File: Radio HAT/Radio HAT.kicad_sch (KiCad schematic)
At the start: 26 parts, among them J1 Raspberry_Pi_2_3, J2 Coax SMA, J3 Barrel_Jack, J4 VCC, J5 6V, J6 GND, U1 RFM98PW, U2 AZ2185D-ADJTRG1

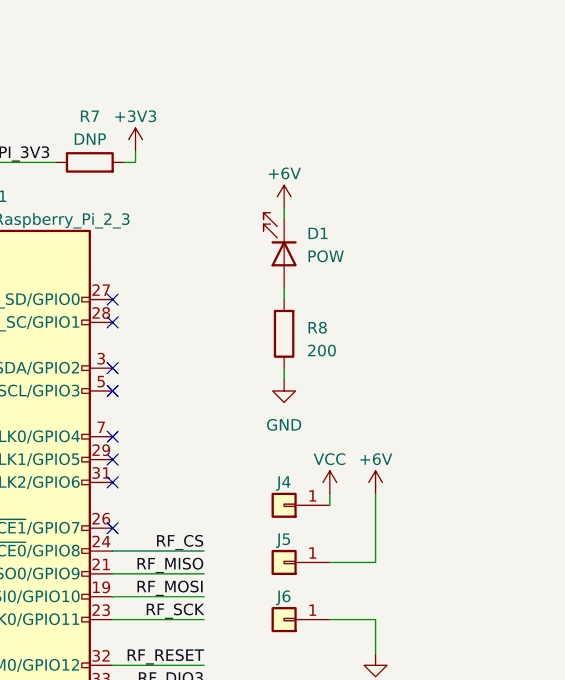
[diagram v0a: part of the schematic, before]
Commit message: Radio HAT v1.1 redesign
Changes:
- Board is back to PWR-GND-SIG-GND
- Made small electrical changes in a lot of spots with Jason
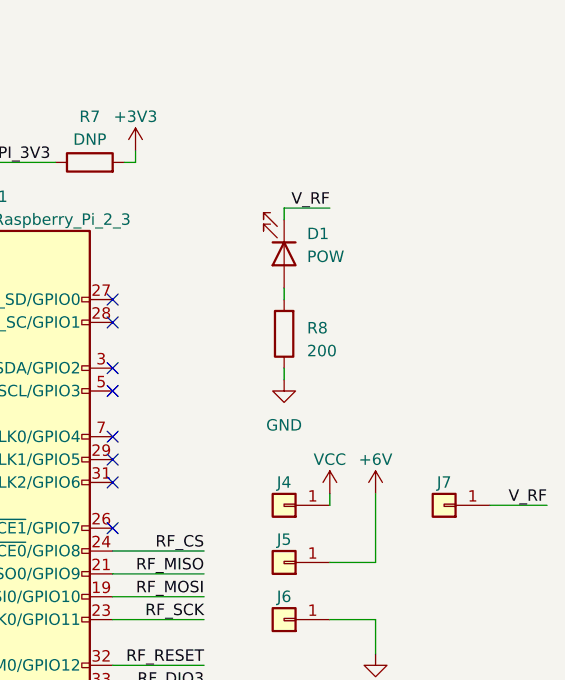
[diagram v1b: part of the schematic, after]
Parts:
- added J7: V_RF, TestPoint:TestPoint_Loop_D2.50mm_Drill1.0mm, symbol Connector_Generic:Conn_01x01
- R5: footprint Resistor_SMD:R_1206_3216Metric_Pad1.30x1.75mm_HandSolder -> Resistor_SMD:R_1210_3225Metric_Pad1.30x2.65mm_HandSolder
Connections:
- net +6V: no longer D1.1 (K)
- net V_RF: now also D1.1 (K), J7.1 (Pin_1)
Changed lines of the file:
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@@
   (title_block
     (title "Argus-1 Ground Station")
-    (date "2023-10-31")
+    (date "2023-11-10")
     (rev "v1.1")
     (company "LICENSE: CC BY 4.0")
@@
     (stroke (width 0) (type default))
   )
+  (wire (pts (xy 217.17 72.39) (xy 222.25 72.39))
+    (stroke (width 0) (type default))
+  )
   (wire (pts (xy 180.34 142.24) (xy 182.88 142.24))
     (stroke (width 0) (type default))
@@
   )
   (wire (pts (xy 147.32 100.33) (xy 157.48 100.33))
+    (stroke (width 0) (type default))
+  )
+  (wire (pts (xy 240.03 105.41) (xy 246.38 105.41))
     (stroke (width 0) (type default))
   )
@@
     (effects (font (size 1.27 1.27)) (justify left bottom))
   )
+  (label "V_RF" (at 246.38 105.41 180) (fields_autoplaced)
+    (effects (font (size 1.27 1.27)) (justify right bottom))
+  )
   (label "RF_DIO3" (at 124.46 119.38 180) (fields_autoplaced)
     (effects (font (size 1.27 1.27)) (justify right bottom))
@@
     (effects (font (size 1.27 1.27)) (justify left bottom))
   )
+  (label "V_RF" (at 222.25 72.39 180) (fields_autoplaced)
+    (effects (font (size 1.27 1.27)) (justify right bottom))
+  )
   (label "RF_DIO0" (at 73.66 129.54 0) (fields_autoplaced)
     (effects (font (size 1.27 1.27)) (justify left bottom))
@@
         (path "/e833ba5c-90ae-4111-9eec-1a872963763a"
           (reference "#PWR011") (unit 1)
+        )
+      )
+    )
+  )
+  (symbol (lib_id "Connector_Generic:Conn_01x01") (at 234.95 105.41 180) (unit 1)
+    (in_bom yes) (on_board yes) (dnp no)
+    (property "Reference" "J7" (at 234.95 102.87 0)
+      (effects (font (size 1.27 1.27)))
+    )
+    (property "Value" "V_RF" (at 234.95 102.87 0)
+      (effects (font (size 1.27 1.27)) hide)
+    )
+    (property "Footprint" "TestPoint:TestPoint_Loop_D2.50mm_Drill1.0mm" (at 234.95 105.41 0)
+      (effects (font (size 1.27 1.27)) hide)
+    )
+    (property "Datasheet" "~" (at 234.95 105.41 0)
+      (effects (font (size 1.27 1.27)) hide)
+    )
+    (pin "1")
+    (instances
+      (project "Radio HAT"
+        (path "/e833ba5c-90ae-4111-9eec-1a872963763a"
+          (reference "J7") (unit 1)
         )
       )
@@
       (effects (font (size 1.27 1.27)))
     )
-    (property "Footprint" "Resistor_SMD:R_1206_3216Metric_Pad1.30x1.75mm_HandSolder" (at 140.97 44.958 90)
+    (property "Footprint" "Resistor_SMD:R_1210_3225Metric_Pad1.30x2.65mm_HandSolder" (at 140.97 44.958 90)
       (effects (font (size 1.27 1.27)) hide)
     )
@@
         )
       )
-    )
-  )
-  (symbol (lib_id "power:+6V") (at 217.17 72.39 0) (unit 1)
-    (in_bom yes) (on_board yes) (dnp no) (fields_autoplaced)
-    (property "Reference" "#PWR027" (at 217.17 76.2 0)
-      (effects (font (size 1.27 1.27)) hide)
-    )
-    (property "Value" "+6V" (at 217.17 68.58 0)
-      (effects (font (size 1.27 1.27)))
-    )
-    (property "Footprint" "" (at 217.17 72.39 0)
-      (effects (font (size 1.27 1.27)) hide)
-    )
-    (property "Datasheet" "" (at 217.17 72.39 0)
-      (effects (font (size 1.27 1.27)) hide)
-    )
-    (pin "1")
-    (instances
-      (project "Radio HAT"
-        (path "/e833ba5c-90ae-4111-9eec-1a872963763a"
-          (reference "#PWR027") (unit 1)
-        )
-      )

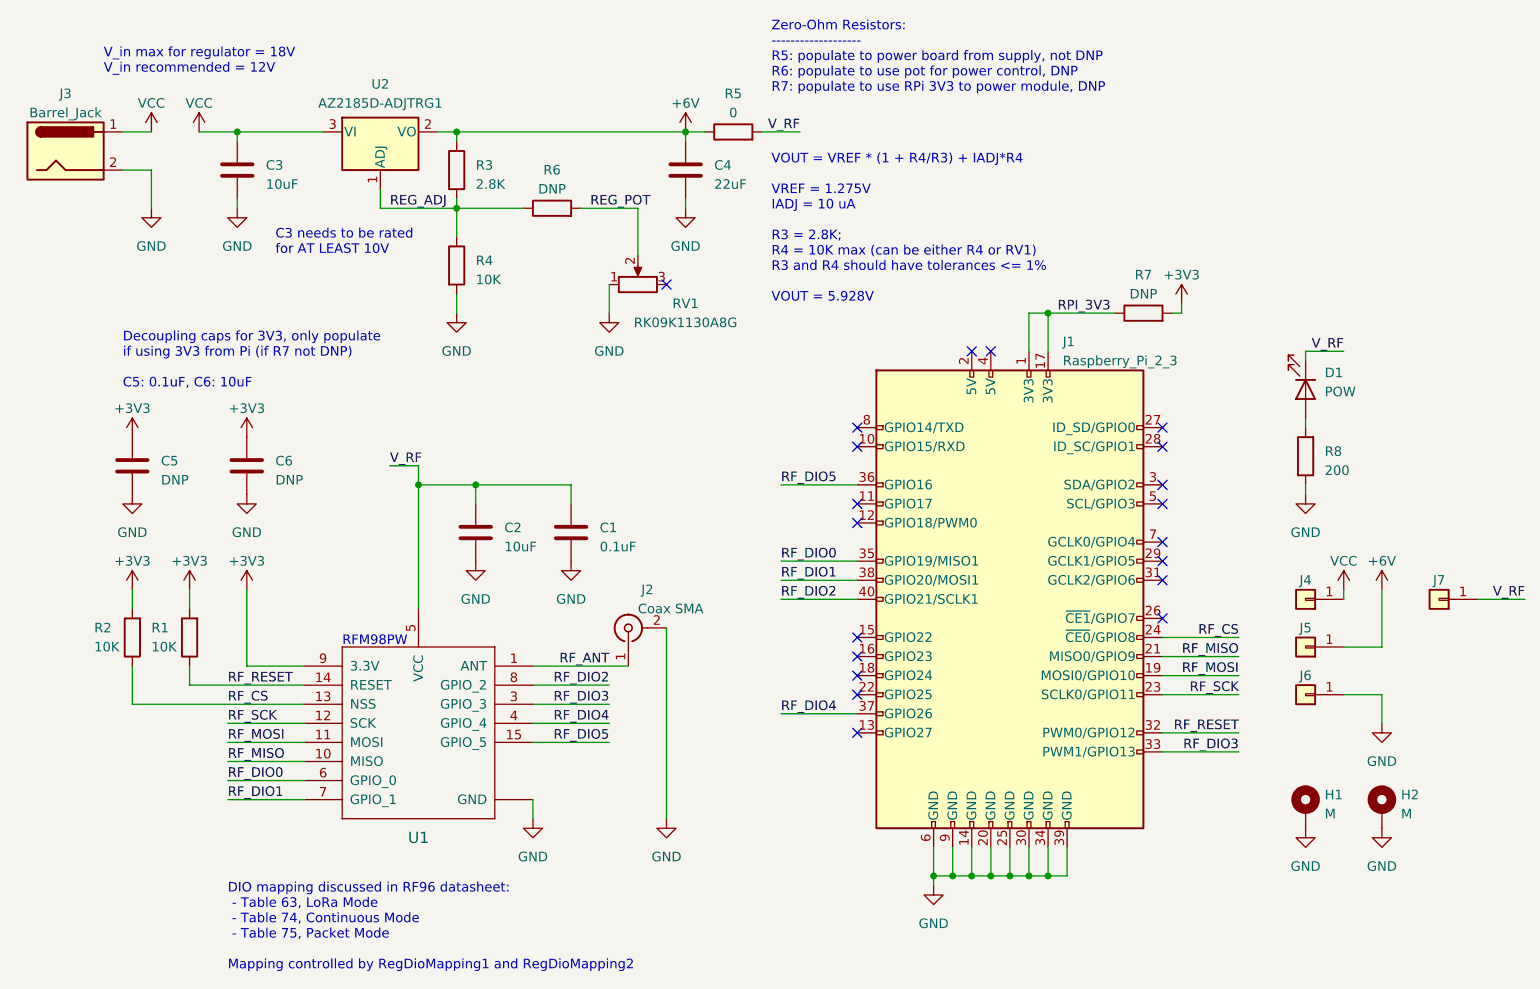
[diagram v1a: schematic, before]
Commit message: Added gerbers, fixed silkscreen overlaps
Minor fixes to fix parts of silkscreen overlapping or crossing into footprints, generated gerber files for v1.1
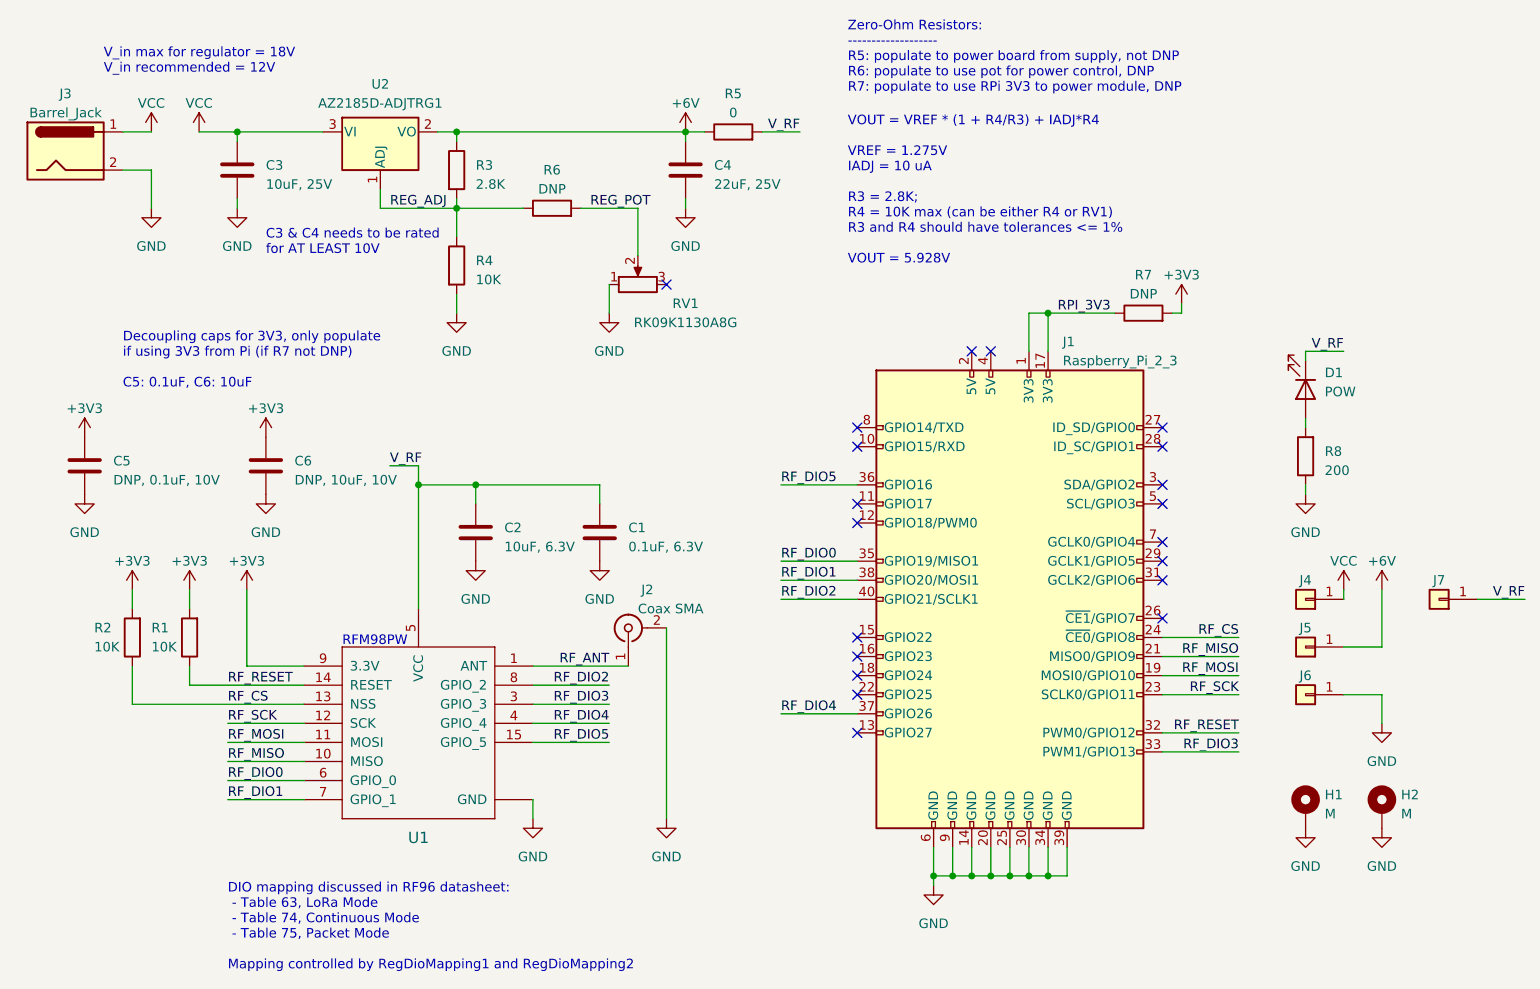
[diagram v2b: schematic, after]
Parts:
- C1: value 0.1uF -> 0.1uF, 6.3V
- C2: value 10uF -> 10uF, 6.3V
- C3: value 10uF -> 10uF, 25V
- C4: value 22uF -> 22uF, 25V
- C5: value DNP -> DNP, 0.1uF, 10V
- C6: value DNP -> DNP, 10uF, 10V
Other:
- note added: "C3 & C4 needs to be rated for AT LEAST 10V"
- note removed: "C3 needs to be rated for AT LEAST 10V"
- moved on the sheet: C1, C5, C6

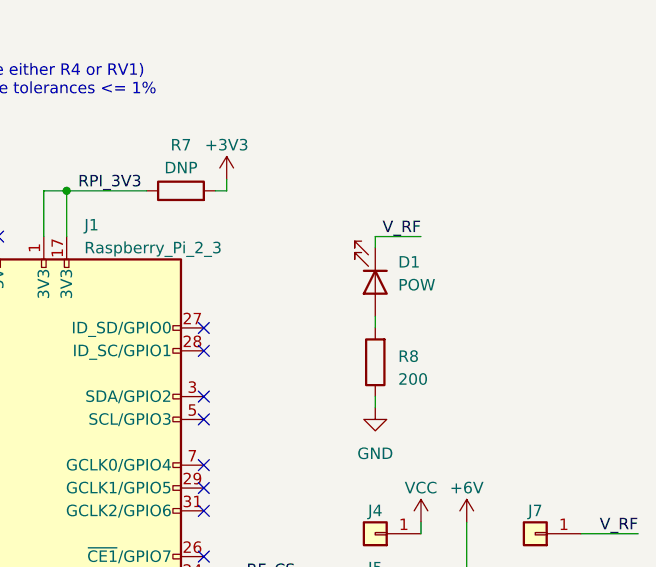
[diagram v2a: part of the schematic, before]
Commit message: Fixed LED placement
LED was initially placed backwards
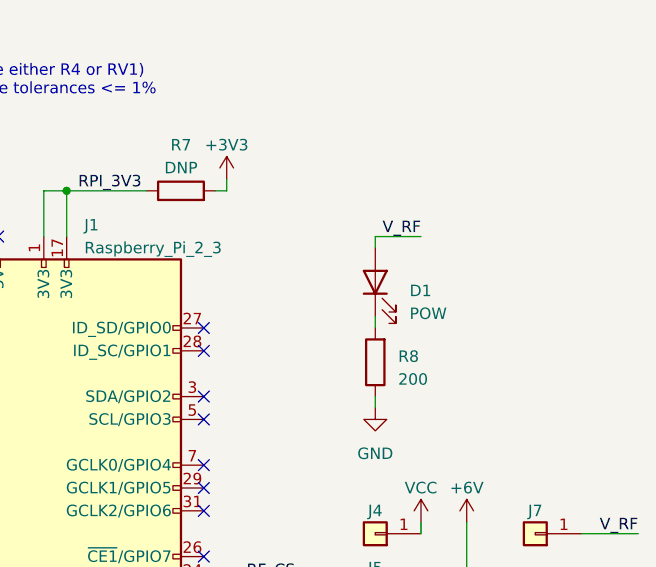
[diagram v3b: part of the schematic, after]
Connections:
- net V_RF: now also D1.2 (A); no longer D1.1 (K)
- net at R8.2: now also D1.1 (K); no longer D1.2 (A)
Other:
- moved on the sheet: D1
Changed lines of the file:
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@@
     )
   )
-  (symbol (lib_id "Device:LED") (at 217.17 77.47 270) (unit 1)
+  (symbol (lib_id "Device:LED") (at 217.17 77.47 90) (unit 1)
     (in_bom yes) (on_board yes) (dnp no) (fields_autoplaced)
-    (property "Reference" "D1" (at 219.71 75.2475 90)
-      (effects (font (size 1.27 1.27)) (justify left))
+    (property "Reference" "D1" (at 220.98 78.4225 90)
+      (effects (font (size 1.27 1.27)) (justify right))
     )
-    (property "Value" "POW" (at 219.71 77.7875 90)
-      (effects (font (size 1.27 1.27)) (justify left))
+    (property "Value" "POW" (at 220.98 80.9625 90)
+      (effects (font (size 1.27 1.27)) (justify right))
     )
     (property "Footprint" "LED_SMD:LED_0805_2012Metric_Pad1.15x1.40mm_HandSolder" (at 217.17 77.47 0)

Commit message: Updated BOM, removed gerbers
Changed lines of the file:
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@@
   )
   (text "Decoupling caps for 3V3, only populate \nif using 3V3 from Pi (if R7 not DNP)\n\nC5: 0.1uF, C6: 10uF"
-    (at 59.69 77.47 0)
+    (at 52.07 77.47 0)
     (effects (font (size 1.27 1.27)) (justify left bottom))
   )
@@
     (effects (font (size 1.27 1.27) (color 0 0 0 1)) (justify left bottom))
   )
-  (text "C3 & C4 needs to be rated\nfor AT LEAST 10V" (at 78.74 59.69 0)
+  (text "C3 & C4 needs to be rated\nfor AT LEAST 10V" (at 72.39 64.77 0)
     (effects (font (size 1.27 1.27)) (justify left bottom))
   )
